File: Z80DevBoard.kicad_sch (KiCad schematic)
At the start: 161 parts, among them J1 Conn_01x02_Pin, SW1 WAIT, SW2 RESET, SW3 Z80BOOT, SW4 RPBOOT, SW5 SW_Nidec_CAS-120A1, SW6 Z80_CLOCK, U1 74HC14, U2 74HC04, U3 74HC00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

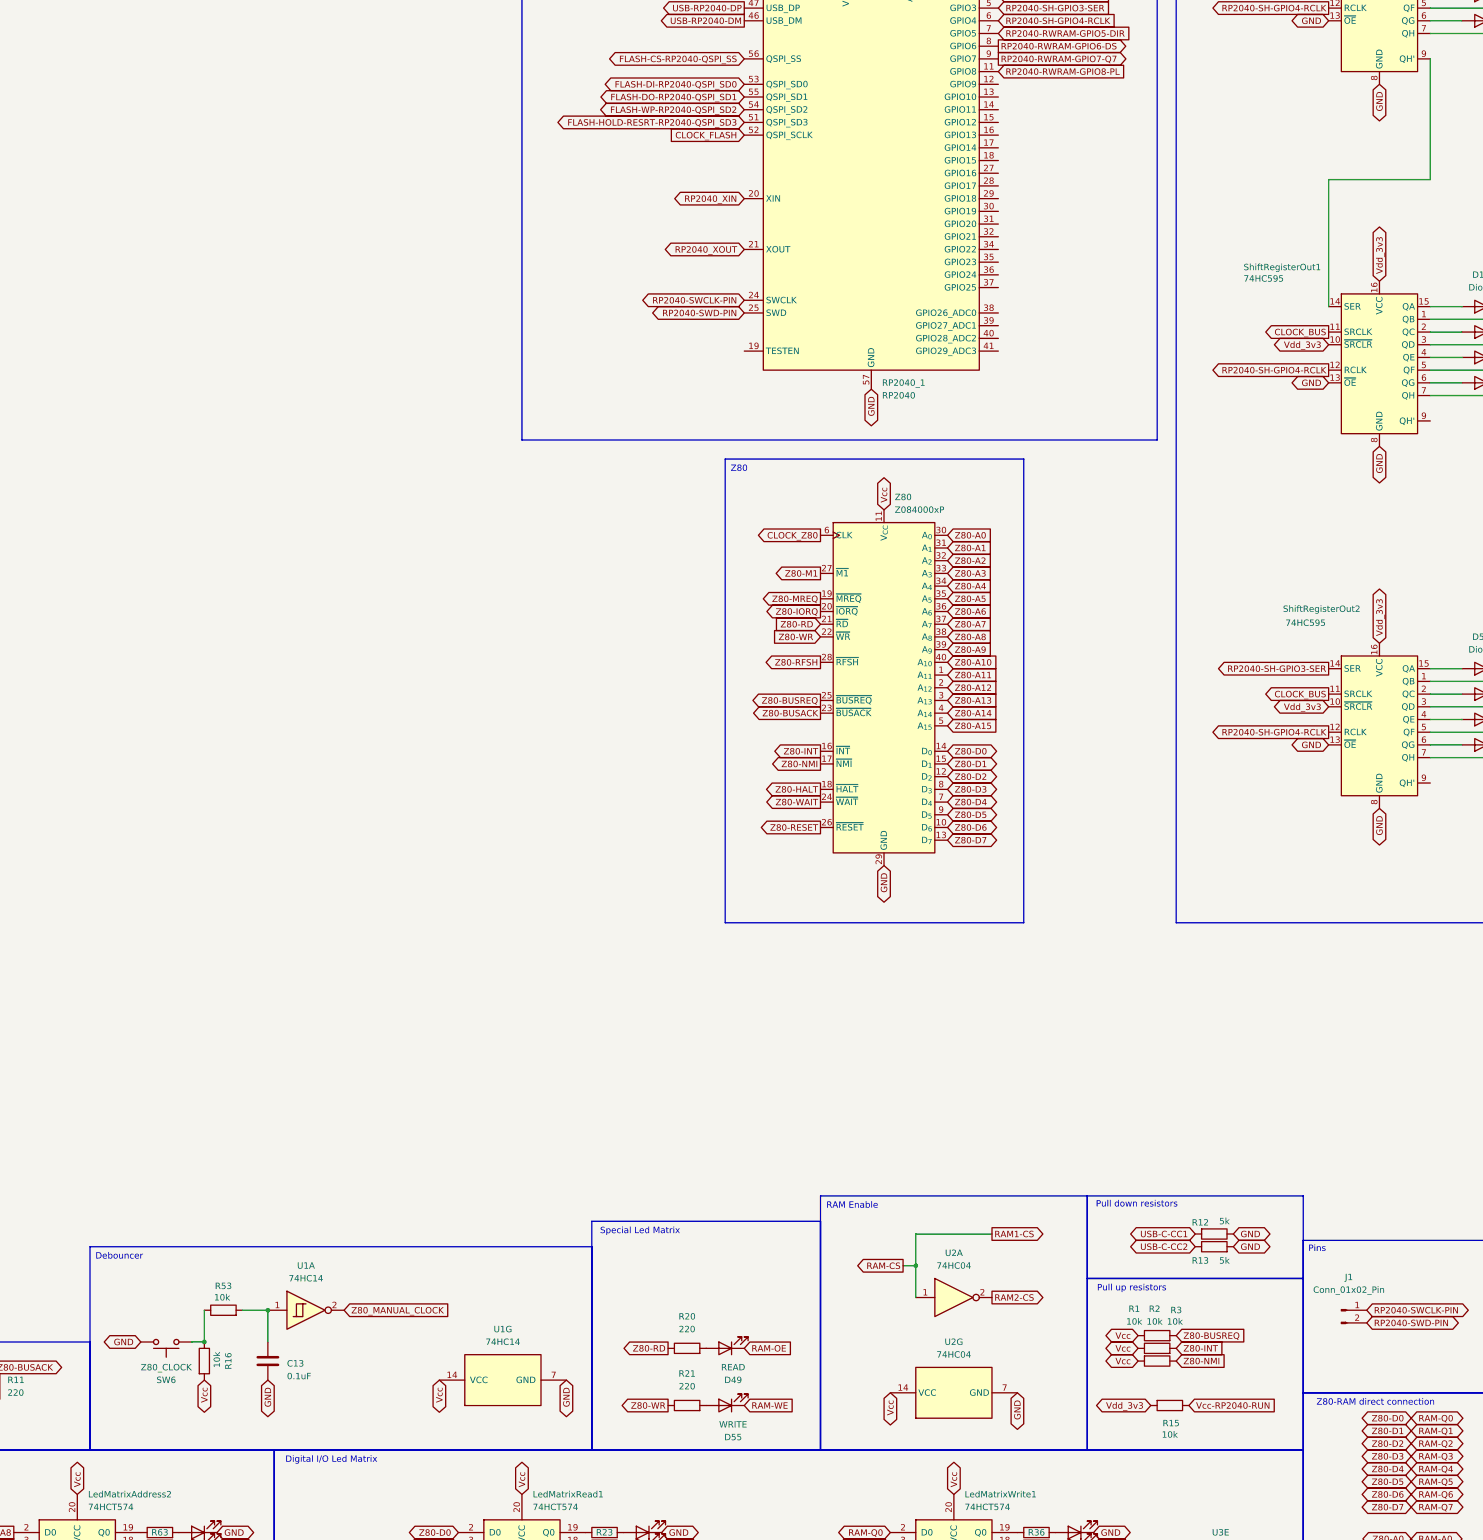
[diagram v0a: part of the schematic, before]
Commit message: Added two pins socket to support expansion boards and advanced projects.
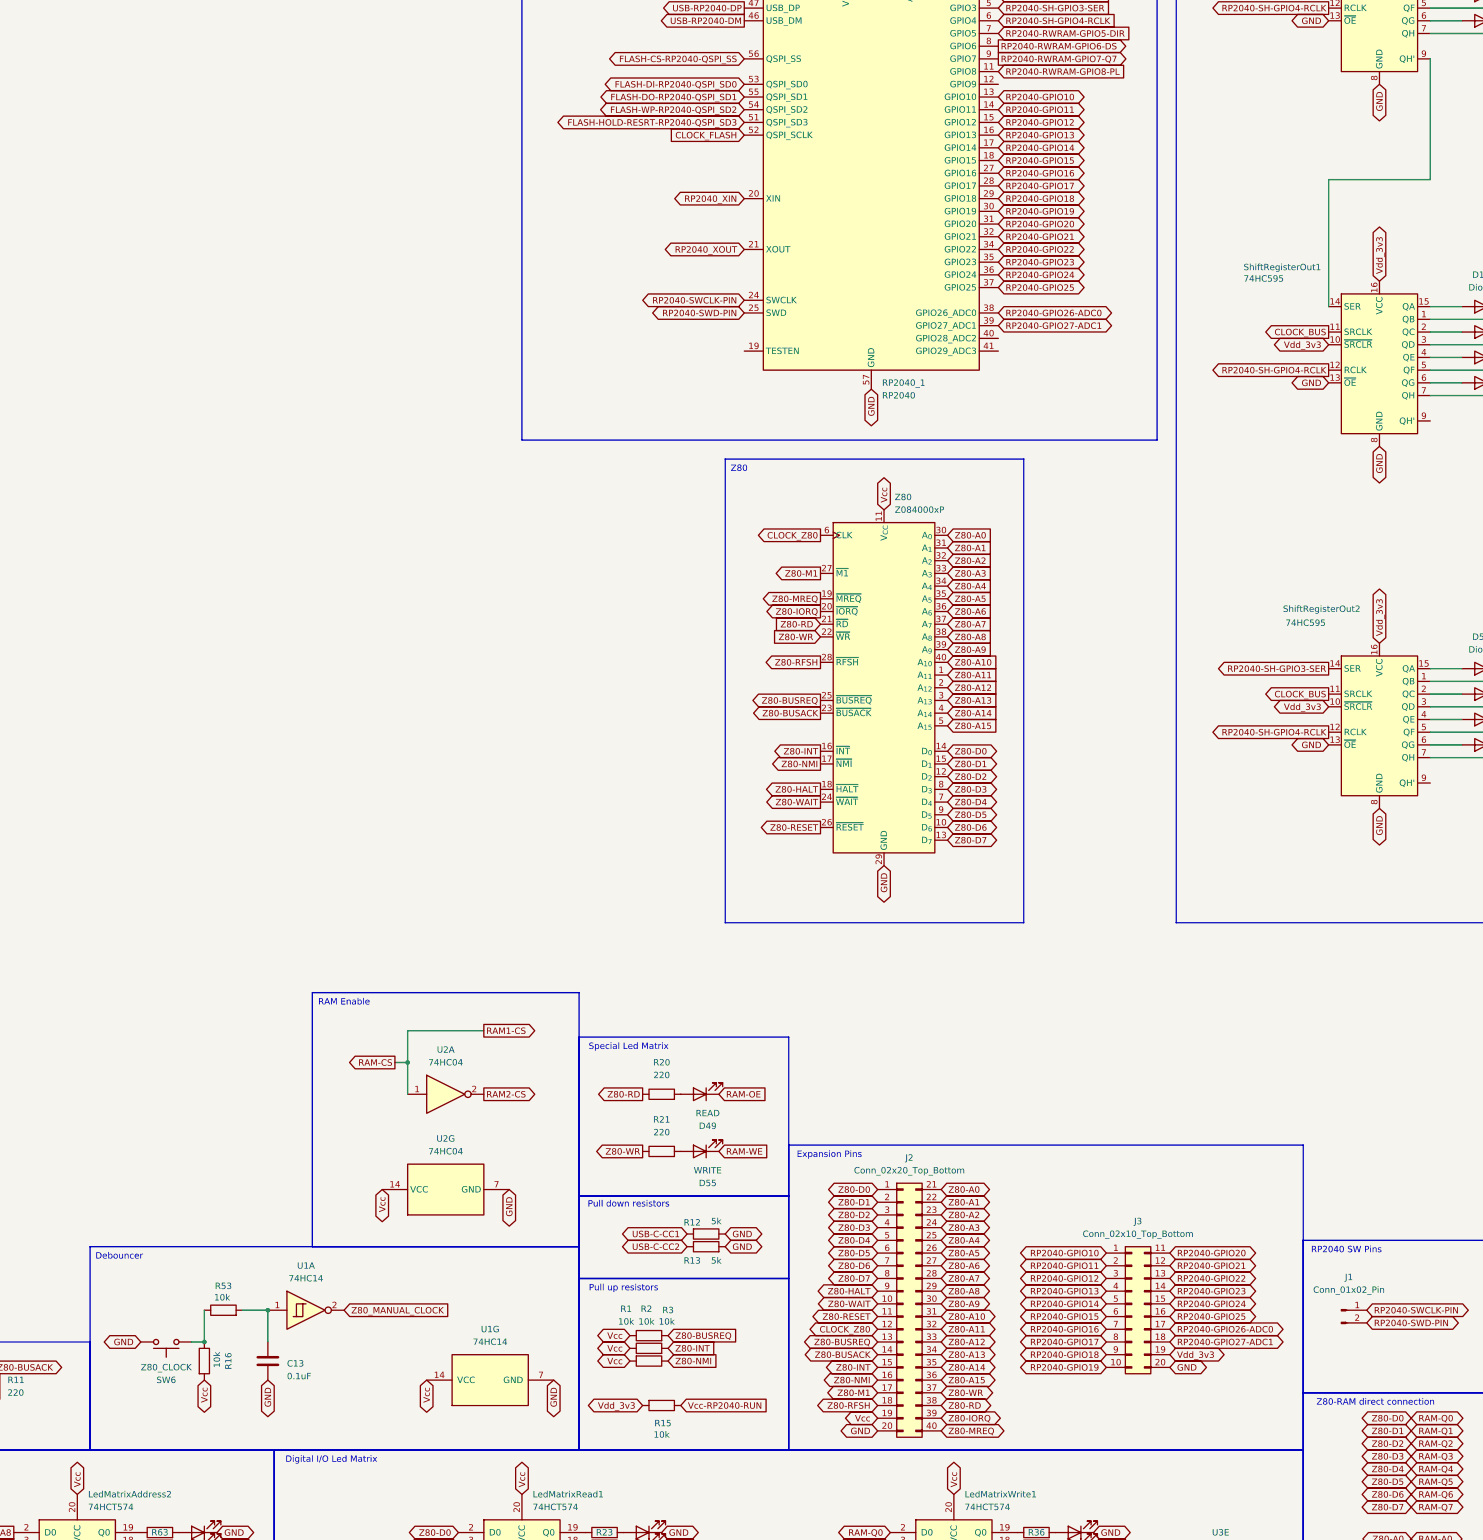
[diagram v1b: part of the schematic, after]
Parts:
- added J2: Conn_02x20_Top_Bottom, Connector_PinSocket_1.27mm:PinSocket_2x20_P1.27mm_Vertical, symbol Connector_Generic:Conn_02x20_Top_Bottom
- added J3: Conn_02x10_Top_Bottom, Connector_PinSocket_1.27mm:PinSocket_2x10_P1.27mm_Vertical, symbol Connector_Generic:Conn_02x10_Top_Bottom
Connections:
- net CLOCK_Z80: now also J2.12 (Pin_12)
- net GND: now also J2.20 (Pin_20), J3.20 (Pin_20)
- net RAM-A0: now also J2.21 (Pin_21)
- net RAM-A1: now also J2.22 (Pin_22)
- net RAM-A10: now also J2.31 (Pin_31)
- net RAM-A11: now also J2.32 (Pin_32)
- net RAM-A12: now also J2.33 (Pin_33)
- net RAM-A13: now also J2.34 (Pin_34)
- net RAM-A14: now also J2.35 (Pin_35)
- net RAM-A2: now also J2.23 (Pin_23)
- net RAM-A3: now also J2.24 (Pin_24)
- net RAM-A4: now also J2.25 (Pin_25)
- net RAM-A5: now also J2.26 (Pin_26)
- net RAM-A6: now also J2.27 (Pin_27)
- net RAM-A7: now also J2.28 (Pin_28)
- net RAM-A8: now also J2.29 (Pin_29)
- net RAM-A9: now also J2.30 (Pin_30)
- net RAM-CS: now also J2.36 (Pin_36)
- net RAM-Q0: now also J2.1 (Pin_1)
- net RAM-Q1: now also J2.2 (Pin_2)
- net RAM-Q2: now also J2.3 (Pin_3)
- net RAM-Q3: now also J2.4 (Pin_4)
- net RAM-Q4: now also J2.5 (Pin_5)
- net RAM-Q5: now also J2.6 (Pin_6)
- net RAM-Q6: now also J2.7 (Pin_7)
- net RAM-Q7: now also J2.8 (Pin_8)
- net Vcc: now also J2.19 (Pin_19)
- net Vdd_3v3: now also J3.19 (Pin_19)
- net Z80-BUSACK: now also J2.14 (Pin_14)
- net Z80-BUSREQ: now also J2.13 (Pin_13)
- net Z80-HALT: now also J2.9 (Pin_9)
- net Z80-INT: now also J2.15 (Pin_15)
- net Z80-IORQ: now also J2.39 (Pin_39)
- net Z80-M1: now also J2.17 (Pin_17)
- net Z80-MREQ: now also J2.40 (Pin_40)
- net Z80-NMI: now also J2.16 (Pin_16)
- net Z80-RD: now also J2.38 (Pin_38)
- net Z80-RESET: now also J2.11 (Pin_11)
- net Z80-RFSH: now also J2.18 (Pin_18)
- net Z80-WAIT: now also J2.10 (Pin_10)
- net Z80-WR: now also J2.37 (Pin_37)
- net RP2040-GPIO10: now reaches RP2040_1.13 (GPIO10)
- net RP2040-GPIO10: now also J3.1 (Pin_1)
- net RP2040-GPIO11: now reaches RP2040_1.14 (GPIO11)
- net RP2040-GPIO11: now also J3.2 (Pin_2)
- net RP2040-GPIO12: now reaches RP2040_1.15 (GPIO12)
- net RP2040-GPIO12: now also J3.3 (Pin_3)
- net RP2040-GPIO13: now reaches RP2040_1.16 (GPIO13)
- net RP2040-GPIO13: now also J3.4 (Pin_4)
- net RP2040-GPIO14: now reaches RP2040_1.17 (GPIO14)
- net RP2040-GPIO14: now also J3.5 (Pin_5)
- net RP2040-GPIO15: now reaches RP2040_1.18 (GPIO15)
- net RP2040-GPIO15: now also J3.6 (Pin_6)
- net RP2040-GPIO16: now reaches RP2040_1.27 (GPIO16)
- net RP2040-GPIO16: now also J3.7 (Pin_7)
- net RP2040-GPIO17: now reaches RP2040_1.28 (GPIO17)
- net RP2040-GPIO17: now also J3.8 (Pin_8)
- net RP2040-GPIO18: now reaches RP2040_1.29 (GPIO18)
- net RP2040-GPIO18: now also J3.9 (Pin_9)
- net RP2040-GPIO19: now reaches RP2040_1.30 (GPIO19)
- net RP2040-GPIO19: now also J3.10 (Pin_10)
- net RP2040-GPIO20: now reaches RP2040_1.31 (GPIO20)
- net RP2040-GPIO20: now also J3.11 (Pin_11)
- net RP2040-GPIO21: now reaches RP2040_1.32 (GPIO21)
- net RP2040-GPIO21: now also J3.12 (Pin_12)
- net RP2040-GPIO22: now reaches RP2040_1.34 (GPIO22)
- net RP2040-GPIO22: now also J3.13 (Pin_13)
- net RP2040-GPIO23: now reaches RP2040_1.35 (GPIO23)
- net RP2040-GPIO23: now also J3.14 (Pin_14)
- net RP2040-GPIO24: now reaches RP2040_1.36 (GPIO24)
- net RP2040-GPIO24: now also J3.15 (Pin_15)
- net RP2040-GPIO25: now reaches RP2040_1.37 (GPIO25)
- net RP2040-GPIO25: now also J3.16 (Pin_16)
- net RP2040-GPIO26-ADC0: now reaches RP2040_1.38 (GPIO26_ADC0)
- net RP2040-GPIO26-ADC0: now also J3.17 (Pin_17)
- net RP2040-GPIO27-ADC1: now reaches RP2040_1.39 (GPIO27_ADC1)
- net RP2040-GPIO27-ADC1: now also J3.18 (Pin_18)
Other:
- note added: "Expansion Pins"
- note added: "RP2040 SW Pins"
- note removed: "Pins"
- moved on the sheet: D49, D55, R1, R12, R13, R15, R2, R20, R21, R3, U1G, U2A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

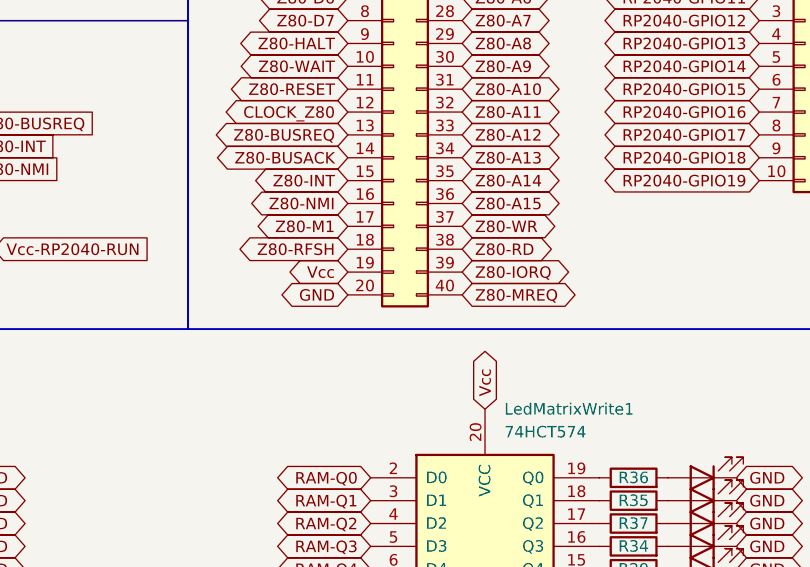
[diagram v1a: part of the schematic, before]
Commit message: Made some connections between the Z80 and the expansion pins. Fixed the GND and Vcc position in the J2 pins.
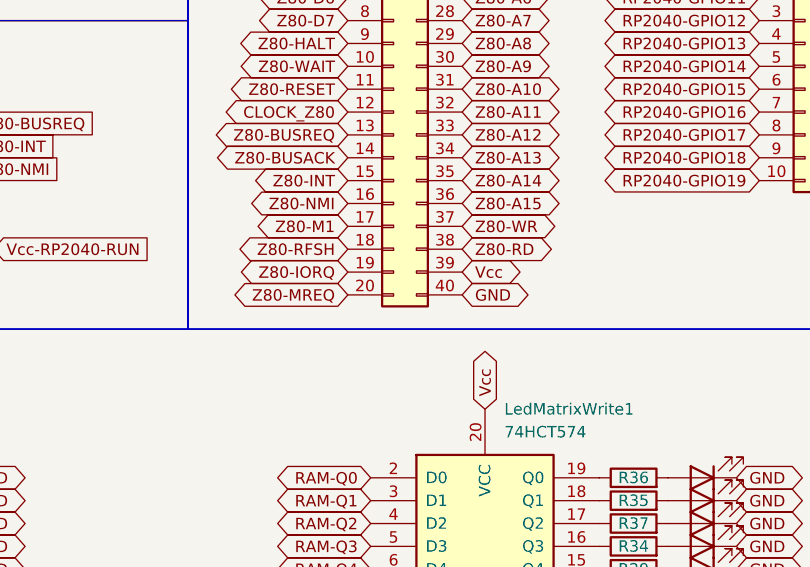
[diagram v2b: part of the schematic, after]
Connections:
- net GND: now also J2.40 (Pin_40); no longer J2.20 (Pin_20)
- net Vcc: now also J2.39 (Pin_39); no longer J2.19 (Pin_19)
- net Z80-IORQ: now also J2.19 (Pin_19); no longer J2.39 (Pin_39)
- net Z80-MREQ: now also J2.20 (Pin_20); no longer J2.40 (Pin_40)
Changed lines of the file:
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@@
 	(title_block
 		(title "Z80DevBoard")
-		(date "2026-03-05")
+		(date "2026-03-10")
 		(company "Gianluca Rainis")
 		(comment 1 "gianluca-rainis on GitHub")
@@
 		)
 	)
-	(global_label "Z80-IORQ"
-		(shape bidirectional)
-		(at 354.33 337.82 0)
-		(fields_autoplaced yes)
-		(effects
-			(font
-				(size 1.27 1.27)
-			)
-			(justify left)
-		)
-		(property "Intersheetrefs" "${INTERSHEET_REFS}"
-			(at 368.1632 337.82 0)
-			(effects
-				(font
-					(size 1.27 1.27)
-				)
-				(justify left)
-				(hide yes)
-			)
-		)
-	)
 	(global_label "RAM-A9"
 		(shape output)
@@
 		)
 	)
+	(global_label "GND"
+		(shape bidirectional)
+		(at 354.33 340.36 0)
+		(fields_autoplaced yes)
+		(effects
+			(font
+				(size 1.27 1.27)
+			)
+			(justify left)
+		)
+		(property "Intersheetrefs" "${INTERSHEET_REFS}"
+			(at 362.297 340.36 0)
+			(effects
+				(font
+					(size 1.27 1.27)
+				)
+				(justify left)
+				(hide yes)
+			)
+		)
+	)
 	(global_label "RAM-A10"
 		(shape bidirectional)
@@
 		)
 	)
-	(global_label "GND"
-		(shape bidirectional)
-		(at 341.63 340.36 180)
-		(fields_autoplaced yes)
-		(effects
-			(font
-				(size 1.27 1.27)
-			)
-			(justify right)
-		)
-		(property "Intersheetrefs" "${INTERSHEET_REFS}"
-			(at 333.663 340.36 0)
-			(effects
-				(font
-					(size 1.27 1.27)
-				)
-				(justify right)
-				(hide yes)
-			)
-		)
-	)
 	(global_label "Z80-RESET"
 		(shape input)
@@
 		)
 	)
+	(global_label "Z80-IORQ"
+		(shape bidirectional)
+		(at 341.63 337.82 180)
+		(fields_autoplaced yes)
+		(effects
+			(font
+				(size 1.27 1.27)
+			)
+			(justify right)
+		)
+		(property "Intersheetrefs" "${INTERSHEET_REFS}"
+			(at 327.7968 337.82 0)
+			(effects
+				(font
+					(size 1.27 1.27)
+				)
+				(justify right)
+				(hide yes)
+			)
+		)
+	)
 	(global_label "Z80-WR"
 		(shape output)
@@
 		)
 	)
+	(global_label "Vcc"
+		(shape bidirectional)
+		(at 354.33 337.82 0)
+		(fields_autoplaced yes)
+		(effects
+			(font
+				(size 1.27 1.27)
+			)
+			(justify left)
+		)
+		(property "Intersheetrefs" "${INTERSHEET_REFS}"
+			(at 361.6923 337.82 0)
+			(effects
+				(font
+					(size 1.27 1.27)
+				)
+				(justify left)
+				(hide yes)
+			)
+		)
+	)
 	(global_label "RP2040-GPIO22"
 		(shape bidirectional)
@@
 	(global_label "Z80-MREQ"
 		(shape bidirectional)
-		(at 354.33 340.36 0)
+		(at 341.63 340.36 180)
 		(fields_autoplaced yes)
 		(effects
@@
 				(size 1.27 1.27)
 			)
-			(justify left)
+			(justify right)
 		)
 		(property "Intersheetrefs" "${INTERSHEET_REFS}"
-			(at 368.8283 340.36 0)
+			(at 327.1317 340.36 0)
 			(effects
 				(font
 					(size 1.27 1.27)
 				)
-				(justify left)
+				(justify right)
 				(hide yes)
 			)
@@
 			(effects
 				(font
-					(size 1.27 1.27)
-				)
-				(justify right)
-				(hide yes)
-			)
-		)
-	)
-	(global_label "Vcc"
-		(shape bidirectional)
-		(at 341.63 337.82 180)
-		(fields_autoplaced yes)
-		(effects
-			(font
-				(size 1.27 1.27)
-			)
-			(justify right)
-		)
-		(property "Intersheetrefs" "${INTERSHEET_REFS}"
-			(at 334.2677 337.82 0)
-			(effects
-				(font

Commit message: Fixed some little details. Updated the bus clock.
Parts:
- SW1, SW2, SW3, SW4: footprint Button_Switch_THT:SW_PUSH_6mm_H7.3mm -> Button_Switch_THT:SW_PUSH_6mm
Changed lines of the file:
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@@
 	(title_block
 		(title "Z80DevBoard")
-		(date "2026-03-10")
+		(date "2026-03-12")
 		(company "Gianluca Rainis")
 		(comment 1 "gianluca-rainis on GitHub")
@@
 			)
 		)
-		(property "Footprint" "Button_Switch_THT:SW_PUSH_6mm_H7.3mm"
+		(property "Footprint" "Button_Switch_THT:SW_PUSH_6mm"
 			(at 36.83 360.68 0)
 			(effects
@@
 			)
 		)
-		(property "Footprint" "Button_Switch_THT:SW_PUSH_6mm_H7.3mm"
+		(property "Footprint" "Button_Switch_THT:SW_PUSH_6mm"
 			(at 36.83 387.35 0)
 			(effects
@@
 			)
 		)
-		(property "Footprint" "Button_Switch_THT:SW_PUSH_6mm_H7.3mm"
+		(property "Footprint" "Button_Switch_THT:SW_PUSH_6mm"
 			(at 67.31 387.35 0)
 			(effects
@@
 			)
 		)
-		(property "Footprint" "Button_Switch_THT:SW_PUSH_6mm_H7.3mm"
+		(property "Footprint" "Button_Switch_THT:SW_PUSH_6mm"
 			(at 67.31 360.68 0)
 			(effects
